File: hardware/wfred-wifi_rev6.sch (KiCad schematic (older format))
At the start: 15 parts, among them J301 Conn_01x02, J302 Conn_01x03, U301 ESP32-S2-WROOM

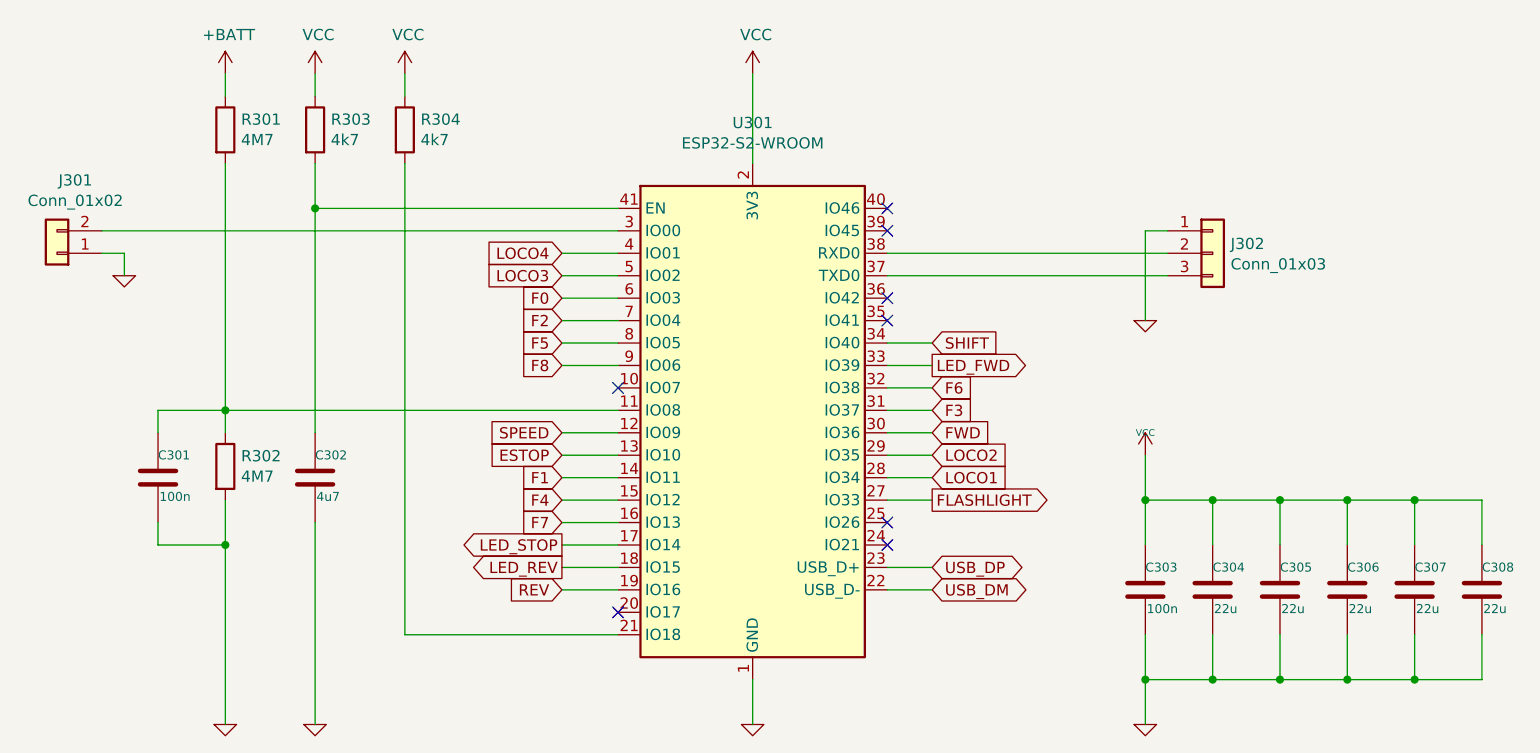
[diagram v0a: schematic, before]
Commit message: Connect USB-C-connector and cleanup
- Replace 2pin + 3pin for RS232 + BOOT with 2x3pin
- Connect USB-C-connector
- Add CC1 and CC2 resistors
- Correct ESP32-S2-WROOM package for hand soldering
- Increase pad sizes for user installed switches / poti
- Correct direction switch pad distance (DRC violation)
- Rearrange some traces and vias
- Add LCSC numbers for pin headers
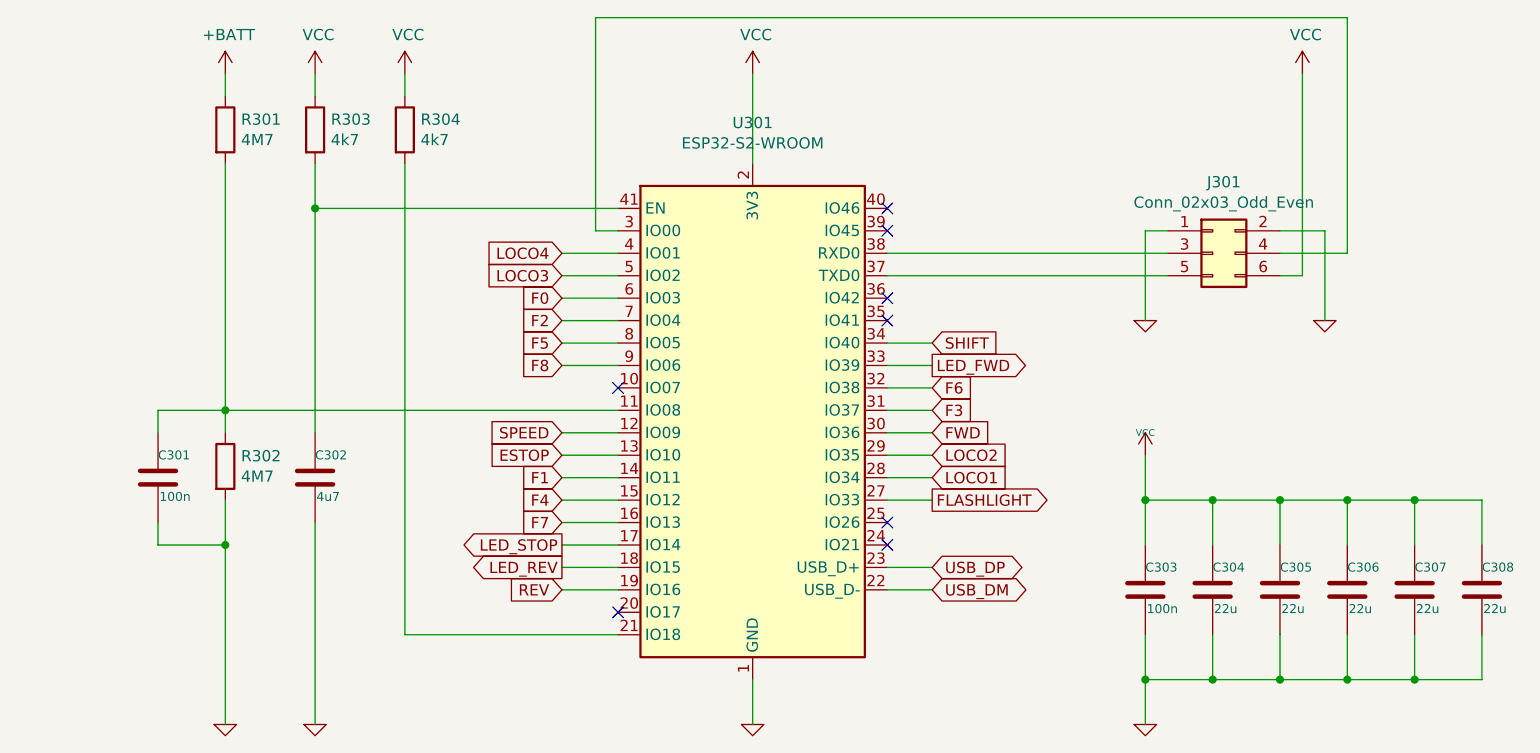
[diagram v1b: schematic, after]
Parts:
- removed J301: Conn_01x02, Connector_PinHeader_2.54mm:PinHeader_1x02_P2.54mm_Vertical, symbol Connector_Generic:Conn_01x02
- removed J302: Conn_01x03, Connector_PinHeader_2.54mm:PinHeader_1x03_P2.54mm_Vertical, symbol Connector_Generic:Conn_01x03
- added J301: Conn_02x03_Odd_Even, Connector_PinHeader_2.54mm:PinHeader_2x03_P2.54mm_Vertical, symbol Connector_Generic:Conn_02x03_Odd_Even
- U301: footprint RF_Module:ESP32-S2-WROVER -> myFootprints:ESP32-S2-WROVER-HandSoldering
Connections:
- net GND: now also J301.1 (Pin_1), J301.2 (Pin_2)
- net VCC: now also J301.6 (Pin_6)
- net at U301.3 (IO00): now also J301.4 (Pin_4)
- net at U301.37 (TXD0): now also J301.5 (Pin_5)
- net at U301.38 (RXD0): now also J301.3 (Pin_3)
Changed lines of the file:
@@
 F 0 "U301" H 5550 5231 50  0000 C CNN
 F 1 "ESP32-S2-WROOM" H 5550 5140 50  0000 C CNN
-F 2 "RF_Module:ESP32-S2-WROVER" H 6300 2700 50  0001 C CNN
+F 2 "myFootprints:ESP32-S2-WROVER-HandSoldering" H 6300 2700 50  0001 C CNN
 F 3 "https://www.espressif.com/sites/default/files/documentation/esp32-s2-wroom_esp32-s2-wroom-i_datasheet_en.pdf" H 5250 3050 50  0001 C CNN
 F 4 "356-ESP32S2WRM3200PH" H 5550 3850 50  0001 C CNN "Mouser"
@@
 Wire Wire Line
 	6150 4550 6350 4550
-$Comp
-L wfred_rev6-rescue:GND-RESCUE-wfred_rev2-wfred_rev2-rescue #PWR0301
-U 1 1 60292B21
-P 2750 3150
-AR Path="/60292B21" Ref="#PWR0301"  Part="1"
-AR Path="/5A122619/60292B21" Ref="#PWR0301"  Part="1"
-F 0 "#PWR0301" H 2750 3150 30  0001 C CNN
-F 1 "GND" H 2750 3080 30  0001 C CNN
-F 2 "" H 2750 3150 60  0001 C CNN
-F 3 "" H 2750 3150 60  0001 C CNN
-	1    2750 3150
-	1    0    0    -1
-$EndComp
-Wire Wire Line
-	2650 3050 2750 3050
-Wire Wire Line
-	2750 3050 2750 3150
-$Comp
-L Connector_Generic:Conn_01x03 J302
-U 1 1 60295C52
-P 7600 3050
-F 0 "J302" H 7680 3092 50  0000 L CNN
-F 1 "Conn_01x03" H 7680 3001 50  0000 L CNN
-F 2 "Connector_PinHeader_2.54mm:PinHeader_1x03_P2.54mm_Vertical" H 7600 3050 50  0001 C CNN
-F 3 "~" H 7600 3050 50  0001 C CNN
-F 4 "SL 1X36G 2,54" H 7600 3050 50  0001 C CNN "Reichelt"
-	1    7600 3050
-	1    0    0    -1
-$EndComp
 Wire Wire Line
 	6150 3050 7400 3050
@@
 Wire Wire Line
 	4700 4550 4950 4550
-$Comp
-L Connector_Generic:Conn_01x02 J301
-U 1 1 60294EB8
-P 2450 3050
-F 0 "J301" H 2368 2725 50  0000 C CNN
-F 1 "Conn_01x02" H 2368 2816 50  0000 C CNN
-F 2 "Connector_PinHeader_2.54mm:PinHeader_1x02_P2.54mm_Vertical" H 2450 3050 50  0001 C CNN
-F 3 "~" H 2450 3050 50  0001 C CNN
-F 4 "SL 1X36G 2,54" H 2450 3050 50  0001 C CNN "Reichelt"
-	1    2450 3050
-	-1   0    0    1
-$EndComp
 Text GLabel 6350 4050 2    50   Input ~ 0
 LOCO1
@@
 	3600 2850 4950 2850
 Wire Wire Line
-	2650 2950 4950 2950
-Wire Wire Line
 	3200 3750 4950 3750
 $Comp
@@
 Wire Wire Line
 	4000 4750 4950 4750
+$Comp
+L Connector_Generic:Conn_02x03_Odd_Even J301
+U 1 1 60C7D9FD
+P 7600 3050
+F 0 "J301" H 7650 3367 50  0000 C CNN
+F 1 "Conn_02x03_Odd_Even" H 7650 3276 50  0000 C CNN
+F 2 "Connector_PinHeader_2.54mm:PinHeader_2x03_P2.54mm_Vertical" H 7600 3050 50  0001 C CNN
+F 3 "~" H 7600 3050 50  0001 C CNN
+F 4 "C358692" H 7600 3050 50  0001 C CNN "LCSC"
+	1    7600 3050
+	1    0    0    -1
+$EndComp
+$Comp
+L wfred_rev6-rescue:GND-RESCUE-wfred_rev2-wfred_rev2-rescue #PWR?
+U 1 1 60C7E0E1
+P 8100 3350
+AR Path="/60C7E0E1" Ref="#PWR?"  Part="1"
+AR Path="/5A122619/60C7E0E1" Ref="#PWR0312"  Part="1"
+F 0 "#PWR0312" H 8100 3350 30  0001 C CNN
+F 1 "GND" H 8100 3280 30  0001 C CNN
+F 2 "" H 8100 3350 60  0001 C CNN
+F 3 "" H 8100 3350 60  0001 C CNN
+	1    8100 3350
+	1    0    0    -1
+$EndComp
+Wire Wire Line
+	8100 3350 8100 2950
+Wire Wire Line
+	8100 2950 7900 2950
+Wire Wire Line
+	7900 3050 8200 3050
+Wire Wire Line
+	8200 3050 8200 2000
+Wire Wire Line
+	8200 2000 4850 2000
+Wire Wire Line
+	4850 2000 4850 2950
+Wire Wire Line
+	4850 2950 4950 2950
+$Comp
+L power:VCC #PWR0301
+U 1 1 60C84260
+P 8000 2250
+F 0 "#PWR0301" H 8000 2100 50  0001 C CNN
+F 1 "VCC" H 8015 2423 50  0000 C CNN
+F 2 "" H 8000 2250 50  0001 C CNN
+F 3 "" H 8000 2250 50  0001 C CNN
+	1    8000 2250
+	1    0    0    -1
+$EndComp
+Wire Wire Line
+	8000 2250 8000 3150
+Wire Wire Line
+	8000 3150 7900 3150
 $EndSCHEMATC
